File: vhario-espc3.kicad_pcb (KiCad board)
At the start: 2 copper layers, 74 x 34 mm, 57 parts, among them J1 USB_C, J2 Battery, Q1 AO3401A, Q2 2N7002, SW1 RST, SW2 DBG, SW3 PWR, SW4 PCCA, U1 cjmcu117, U2 MCP73831-2-OT, U3 espc3fn4, U4 74HC240PWR, U5 TLV75533PDBV

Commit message: optimize tracks
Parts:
- moved BZ1 0.53 mm to (143.8, 71.3)
- moved R16 0.48 mm to (145.9, 70.3)
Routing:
- net /AUDIO: track 51.3 -> 52.0 mm
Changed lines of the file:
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@@
   )
   (footprint "0-vhario-espc3:conn_smd_1x2_2mm" (layer "B.Cu")
-    (at 143.8 71.825)
+    (at 143.8 71.3)
     (property "Sheetfile" "vhario-espc3.kicad_sch")
     (property "Sheetname" "")
@@
   )
   (footprint "0-vhario-espc3:R_0603_1608Metric_Pad0.98x0.95mm_HandSolder" (layer "B.Cu")
-    (at 145.875 70.775 90)
+    (at 145.9 70.3 90)
     (descr "Resistor SMD 0603 (1608 Metric), square (rectangular) end terminal, IPC_7351 nominal with elongated pad for handsoldering. (Body size source: IPC-SM-782 page 72, https://www.pcb-3d.com/wordpress/wp-content/uploads/ipc-sm-782a_amendment_1_and_2.pdf), generated with kicad-footprint-generator")
     (tags "resistor handsolder")
@@
   (segment (start 151.3675 74.575) (end 150.7175 74.575) (width 0.4) (layer "B.Cu") (net 1))
   (segment (start 153.9675 74.575) (end 153.3175 74.575) (width 0.4) (layer "B.Cu") (net 1))
+  (segment (start 143.8875 71.2125) (end 143.8 71.3) (width 0.4) (layer "B.Cu") (net 1))
   (segment (start 154.6175 74.575) (end 153.9675 74.575) (width 0.4) (layer "B.Cu") (net 1))
   (segment (start 152.0175 74.575) (end 151.3675 74.575) (width 0.4) (layer "B.Cu") (net 1))
   (segment (start 153.3175 74.575) (end 152.6675 74.575) (width 0.4) (layer "B.Cu") (net 1))
-  (segment (start 145.875 71.6875) (end 143.9375 71.6875) (width 0.4) (layer "B.Cu") (net 1))
   (segment (start 150.7175 74.575) (end 150.0675 74.575) (width 0.4) (layer "B.Cu") (net 1))
   (segment (start 152.6675 74.575) (end 152.0175 74.575) (width 0.4) (layer "B.Cu") (net 1))
   (segment (start 151.3675 73.1325) (end 151.4 73.1) (width 0.4) (layer "B.Cu") (net 1))
-  (segment (start 147.0375 71.6875) (end 145.875 71.6875) (width 0.4) (layer "B.Cu") (net 1))
-  (segment (start 143.9375 71.6875) (end 143.8 71.825) (width 0.4) (layer "B.Cu") (net 1))
+  (segment (start 145.9 71.2125) (end 143.8875 71.2125) (width 0.4) (layer "B.Cu") (net 1))
+  (segment (start 146.6625 71.2125) (end 147.125 71.675) (width 0.4) (layer "B.Cu") (net 1))
+  (segment (start 145.9 71.2125) (end 146.6625 71.2125) (width 0.4) (layer "B.Cu") (net 1))
   (segment (start 151.3675 74.575) (end 151.3675 73.1325) (width 0.4) (layer "B.Cu") (net 1))
   (segment (start 152.6675 67.7825) (end 152.8 67.65) (width 0.4) (layer "B.Cu") (net 2))
   (segment (start 153.9675 68.775) (end 153.9675 68.1425) (width 0.4) (layer "B.Cu") (net 2))
+  (segment (start 145.9 68.4) (end 145.9 69.3875) (width 0.4) (layer "B.Cu") (net 2))
   (segment (start 151.3675 67.7425) (end 151.275 67.65) (width 0.4) (layer "B.Cu") (net 2))
-  (segment (start 143.8375 69.8625) (end 143.8 69.825) (width 0.4) (layer "B.Cu") (net 2))
   (segment (start 150.3 67.65) (end 150.0675 67.8825) (width 0.4) (layer "B.Cu") (net 2))
-  (segment (start 145.875 69.8625) (end 148.0875 67.65) (width 0.4) (layer "B.Cu") (net 2))
+  (segment (start 150.3 67.65) (end 146.65 67.65) (width 0.4) (layer "B.Cu") (net 2))
   (segment (start 152.8 67.65) (end 151.275 67.65) (width 0.4) (layer "B.Cu") (net 2))
   (segment (start 150.0675 67.8825) (end 150.0675 68.775) (width 0.4) (layer "B.Cu") (net 2))
+  (segment (start 143.8875 69.3875) (end 143.8 69.3) (width 0.4) (layer "B.Cu") (net 2))
+  (segment (start 146.65 67.65) (end 145.9 68.4) (width 0.4) (layer "B.Cu") (net 2))
   (segment (start 151.3675 68.775) (end 151.3675 67.7425) (width 0.4) (layer "B.Cu") (net 2))
   (segment (start 152.6675 68.775) (end 152.6675 67.7825) (width 0.4) (layer "B.Cu") (net 2))
   (segment (start 151.275 67.65) (end 150.3 67.65) (width 0.4) (layer "B.Cu") (net 2))
-  (segment (start 148.0875 67.65) (end 150.3 67.65) (width 0.4) (layer "B.Cu") (net 2))
-  (segment (start 145.875 69.8625) (end 143.8375 69.8625) (width 0.4) (layer "B.Cu") (net 2))
+  (segment (start 145.9 69.3875) (end 143.8875 69.3875) (width 0.4) (layer "B.Cu") (net 2))
   (segment (start 153.475 67.65) (end 152.8 67.65) (width 0.4) (layer "B.Cu") (net 2))
   (segment (start 153.9675 68.1425) (end 153.475 67.65) (width 0.4) (layer "B.Cu") (net 2))
@@
   (segment (start 132.37 90.4) (end 132.65 90.12) (width 0.3) (layer "F.Cu") (net 39))
   (segment (start 106.25 89.42) (end 112.92 89.42) (width 0.3) (layer "F.Cu") (net 39))
+  (segment (start 131.8 71.075) (end 129.425 73.45) (width 0.3) (layer "F.Cu") (net 40))
+  (segment (start 145.175 70.35) (end 144.45 71.075) (width 0.3) (layer "F.Cu") (net 40))
+  (segment (start 150.7 70.35) (end 145.175 70.35) (width 0.3) (layer "F.Cu") (net 40))
+  (segment (start 112.375 73.45) (end 111.25 74.575) (width 0.3) (layer "F.Cu") (net 40))
+  (segment (start 111.25 74.575) (end 111.25 75.92) (width 0.3) (layer "F.Cu") (net 40))
   (segment (start 129.425 73.45) (end 112.375 73.45) (width 0.3) (layer "F.Cu") (net 40))
-  (segment (start 112.375 73.45) (end 111.25 74.575) (width 0.3) (layer "F.Cu") (net 40))
-  (segment (start 149.8 70.35) (end 145.175 70.35) (width 0.3) (layer "F.Cu") (net 40))
-  (segment (start 131.8 71.075) (end 129.425 73.45) (width 0.3) (layer "F.Cu") (net 40))
   (segment (start 144.45 71.075) (end 131.8 71.075) (width 0.3) (layer "F.Cu") (net 40))
-  (segment (start 145.175 70.35) (end 144.45 71.075) (width 0.3) (layer "F.Cu") (net 40))
-  (segment (start 111.25 74.575) (end 111.25 75.92) (width 0.3) (layer "F.Cu") (net 40))
-  (via (at 149.8 70.35) (size 0.8) (drill 0.4) (layers "F.Cu" "B.Cu") (net 40))
-  (segment (start 149.4175 68.775) (end 149.4175 69.9675) (width 0.4) (layer "B.Cu") (net 40))
+  (via (at 150.7 70.35) (size 0.8) (drill 0.4) (layers "F.Cu" "B.Cu") (net 40))
+  (segment (start 150.1425 70.35) (end 149.4175 69.625) (width 0.4) (layer "B.Cu") (net 40))
   (segment (start 152.075 70.35) (end 152.6425 70.35) (width 0.4) (layer "B.Cu") (net 40))
   (segment (start 153.3175 68.775) (end 153.325 68.7825) (width 0.4) (layer "B.Cu") (net 40))
   (segment (start 153.325 69.6675) (end 152.6425 70.35) (width 0.4) (layer "B.Cu") (net 40))
-  (segment (start 149.8 70.35) (end 150.7 70.35) (width 0.4) (layer "B.Cu") (net 40))
   (segment (start 152.0175 68.775) (end 152.0175 70.2925) (width 0.4) (layer "B.Cu") (net 40))
+  (segment (start 149.4175 69.625) (end 149.4175 68.775) (width 0.4) (layer "B.Cu") (net 40))
   (segment (start 150.7175 68.775) (end 150.7175 70.3325) (width 0.4) (layer "B.Cu") (net 40))
+  (segment (start 150.7 70.35) (end 150.1425 70.35) (width 0.4) (layer "B.Cu") (net 40))
   (segment (start 153.325 68.7825) (end 153.325 69.6675) (width 0.4) (layer "B.Cu") (net 40))
-  (segment (start 149.4175 69.9675) (end 149.8 70.35) (width 0.4) (layer "B.Cu") (net 40))
   (segment (start 152.0175 70.2925) (end 152.075 70.35) (width 0.4) (layer "B.Cu") (net 40))
   (segment (start 150.7 70.35) (end 152.075 70.35) (width 0.4) (layer "B.Cu") (net 40))

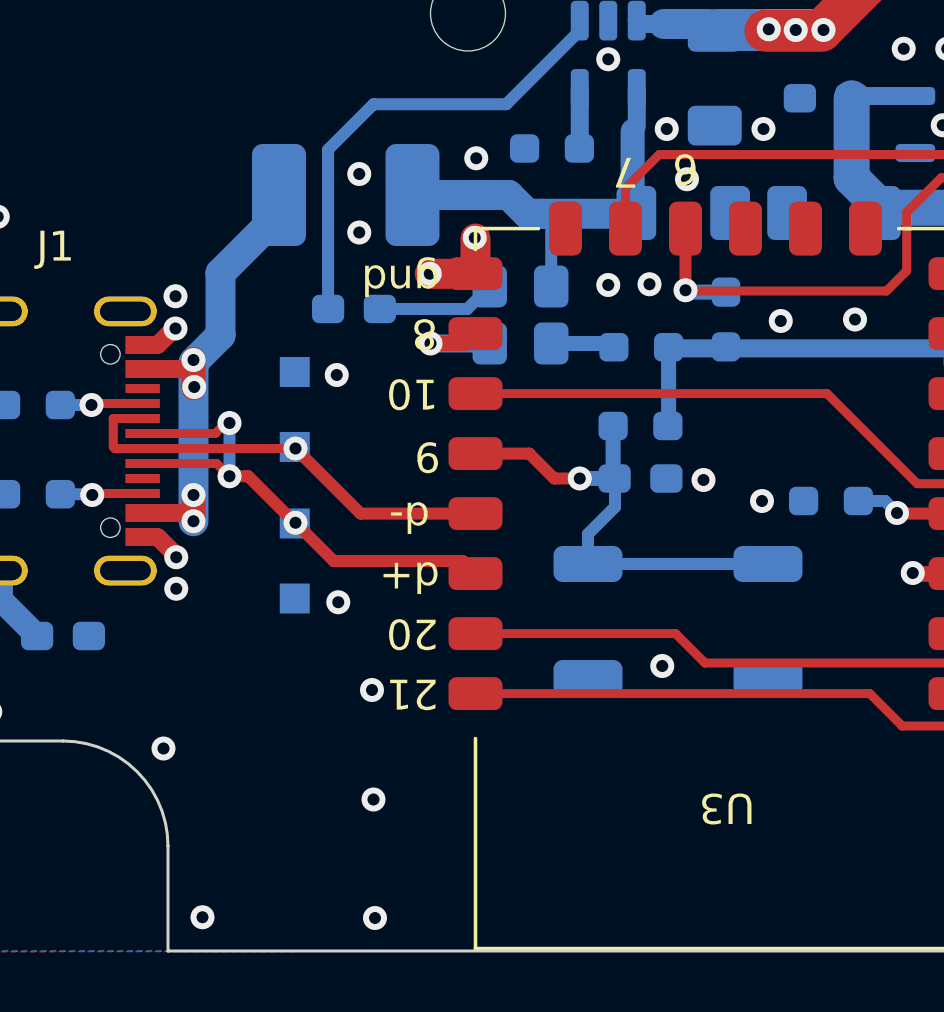
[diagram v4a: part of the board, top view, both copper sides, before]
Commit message: move via out of pad, cleanup silkscreen
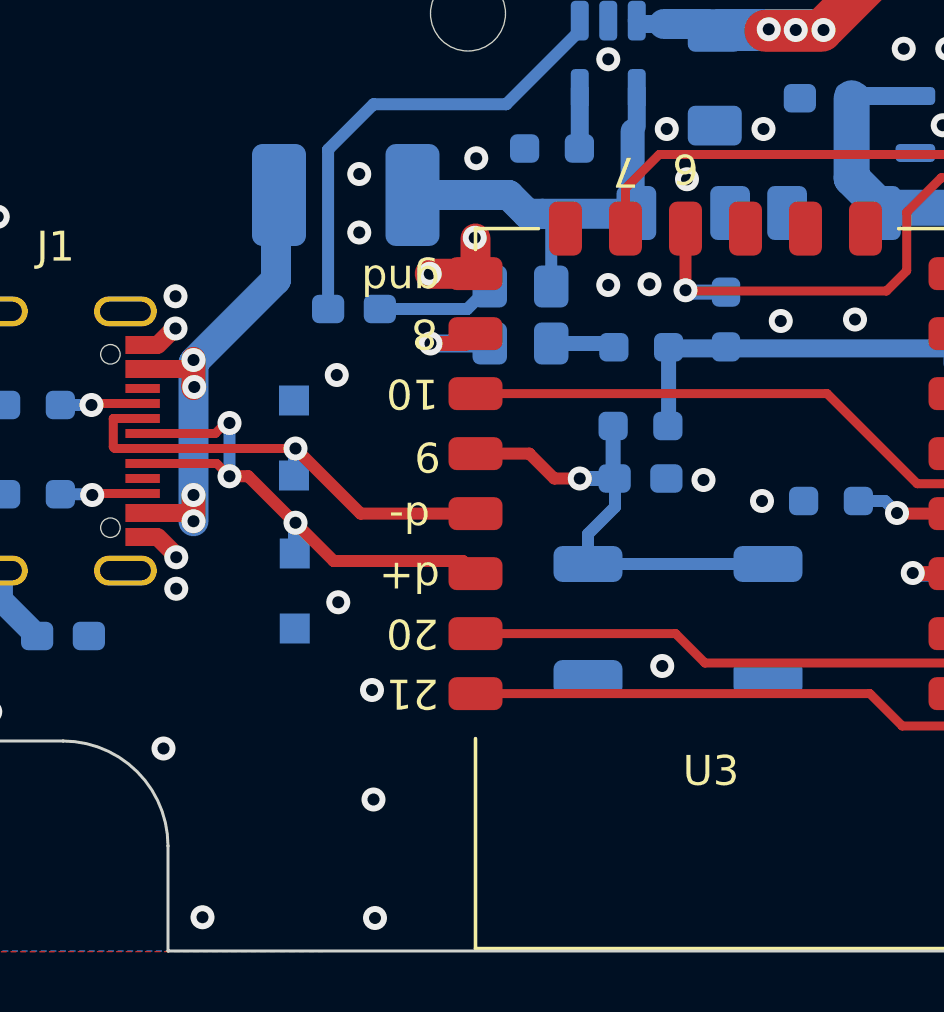
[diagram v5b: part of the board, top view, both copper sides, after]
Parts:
- moved D6 1.00 mm to (100.2, 88.0)
- moved D4 0.95 mm to (100.2, 82.9)
- renumbered SW4 to PCCA, SW3 to PWR, SW1 to RST
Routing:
- net /D+: track 16.9 -> 18.0 mm
- net /D-: track 14.4 -> 15.3 mm
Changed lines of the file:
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@@
     (property "Sheetname" "")
     (attr smd)
-    (fp_text reference "U3" (at 7.62 -3.81 180 unlocked) (layer "F.SilkS")
+    (fp_text reference "U3" (at 8.15 -2.58 unlocked) (layer "F.SilkS")
       (effects (font (size 1 1) (thickness 0.15)))
     )
@@
   )
   (footprint "0-vhario-espc3:D_SOD-323_HandSoldering" (layer "B.Cu")
-    (at 100.225 87 -90)
+    (at 100.225 88 -90)
     (descr "SOD-323")
     (tags "SOD-323")
@@
     (property "Sheetname" "")
     (attr smd)
-    (fp_text reference "D6" (at 0.125 -2.175 180) (layer "B.SilkS")
+    (fp_text reference "D6" (at 0.2 2.025 180) (layer "B.SilkS")
       (effects (font (size 1 1) (thickness 0.15)) (justify mirror))
     )
@@
   )
   (footprint "0-vhario-espc3:D_SOD-323_HandSoldering" (layer "B.Cu")
-    (at 100.225 81.95 90)
+    (at 100.2 82.9 90)
     (descr "SOD-323")
     (tags "SOD-323")
@@
     (property "Sheetname" "")
     (attr smd)
-    (fp_text reference "SW3" (at 0.1 4 unlocked) (layer "B.SilkS")
+    (fp_text reference "PWR" (at 0.1 4 unlocked) (layer "B.SilkS")
       (effects (font (size 1 1) (thickness 0.15)) (justify mirror))
     )
@@
     (property "Sheetname" "")
     (attr smd)
-    (fp_text reference "SW4" (at -3.825 0.075 unlocked) (layer "B.SilkS")
+    (fp_text reference "PCCA" (at -4.2 0 unlocked) (layer "B.SilkS")
       (effects (font (size 1 1) (thickness 0.15)) (justify mirror))
     )
@@
     (property "Sheetname" "")
     (attr smd)
-    (fp_text reference "SW1" (at 4.025 -0.05 unlocked) (layer "B.SilkS")
+    (fp_text reference "RST" (at 4.025 -0.05 unlocked) (layer "B.SilkS")
       (effects (font (size 1 1) (thickness 0.15)) (justify mirror))
     )
@@
   (via (at 96.85 80.3) (size 0.8) (drill 0.4) (layers "F.Cu" "B.Cu") (free) (net 15))
   (via (at 96.875 81.2) (size 0.8) (drill 0.4) (layers "F.Cu" "B.Cu") (free) (net 15))
-  (segment (start 97.75 79.475) (end 97.75 77.4) (width 1) (layer "B.Cu") (net 15))
   (segment (start 96.85 80.4) (end 96.875 80.375) (width 1) (layer "B.Cu") (net 15))
-  (segment (start 97.75 77.4) (end 99.7 75.45) (width 1) (layer "B.Cu") (net 15))
+  (segment (start 96.9 80.325) (end 99.6 77.625) (width 1) (layer "B.Cu") (net 15))
+  (segment (start 99.6 77.625) (end 99.6 74.9) (width 1) (layer "B.Cu") (net 15))
+  (segment (start 99.6 74.9) (end 99.7 74.8) (width 1) (layer "B.Cu") (net 15))
   (segment (start 96.85 85.675) (end 96.85 80.4) (width 1) (layer "B.Cu") (net 15))
-  (segment (start 99.7 75.45) (end 99.7 74.8) (width 1) (layer "B.Cu") (net 15))
-  (segment (start 96.9 80.325) (end 97.75 79.475) (width 1) (layer "B.Cu") (net 15))
   (segment (start 105.975 78.6) (end 106.725 77.85) (width 0.4) (layer "B.Cu") (net 16))
   (segment (start 103.0625 78.6) (end 105.975 78.6) (width 0.4) (layer "B.Cu") (net 16))
@@
   (segment (start 94.23 83.25) (end 94.175 83.195) (width 0.3) (layer "F.Cu") (net 19))
   (via (at 100.25 83.25) (size 0.8) (drill 0.4) (layers "F.Cu" "B.Cu") (net 19))
+  (segment (start 100.25 83.25) (end 100.25 84.1) (width 0.5) (layer "B.Cu") (net 19))
+  (segment (start 100.25 84.1) (end 100.2 84.15) (width 0.4) (layer "B.Cu") (net 19))
   (segment (start 147.65 94.275) (end 148.825 95.45) (width 0.4) (layer "F.Cu") (net 20))
   (segment (start 143.4 95.225) (end 144.35 94.275) (width 0.4) (layer "F.Cu") (net 20))
@@
   (via (at 100.25 85.725) (size 0.8) (drill 0.4) (layers "F.Cu" "B.Cu") (net 21))
   (segment (start 98.05 82.4) (end 98.05 84.175) (width 0.4) (layer "B.Cu") (net 21))
+  (segment (start 100.25 86.725) (end 100.225 86.75) (width 0.4) (layer "B.Cu") (net 21))
+  (segment (start 100.25 85.725) (end 100.25 86.725) (width 0.5) (layer "B.Cu") (net 21))
   (segment (start 93.35 81.75) (end 95.155 81.75) (width 0.3) (layer "F.Cu") (net 23))
   (via (at 93.45 81.8) (size 0.8) (drill 0.4) (layers "F.Cu" "B.Cu") (net 23))
